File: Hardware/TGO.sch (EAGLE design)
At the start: 33 parts, among them J4 SMD_PAD, U1 AP3012, U2 SAS1-1U001-A_I2C_4WSPI

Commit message: Finish prototype v01
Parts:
- removed LOGO1: SFE_LOGO_NAME_FLAME.1_INCH, SparkFun-Aesthetics:SFE_LOGO_NAME_FLAME.1_INCH
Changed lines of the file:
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@@
 <part name="FD2" library="SparkFun-Aesthetics" deviceset="FIDUCIAL" device="1X2"/>
 <part name="FD4" library="SparkFun-Aesthetics" deviceset="FIDUCIAL" device="1X2"/>
-<part name="LOGO1" library="SparkFun-Aesthetics" deviceset="SFE_LOGO_NAME_FLAME" device=".1_INCH"/>
 <part name="LOGO2" library="SparkFun-Aesthetics" deviceset="OSHW-LOGO" device="S"/>
 <part name="J3" library="SparkFun-Connectors" deviceset="CONN_06" device="NO_SILK_NO_POP"/>
@@
 <instance part="FD2" gate="G$1" x="243.84" y="30.48"/>
 <instance part="FD4" gate="G$1" x="246.38" y="30.48"/>
-<instance part="LOGO1" gate="G$1" x="152.4" y="48.26"/>
 <instance part="LOGO2" gate="G$1" x="228.6" y="60.96"/>
 <instance part="J3" gate="G$1" x="111.76" y="22.86" rot="R180"/>

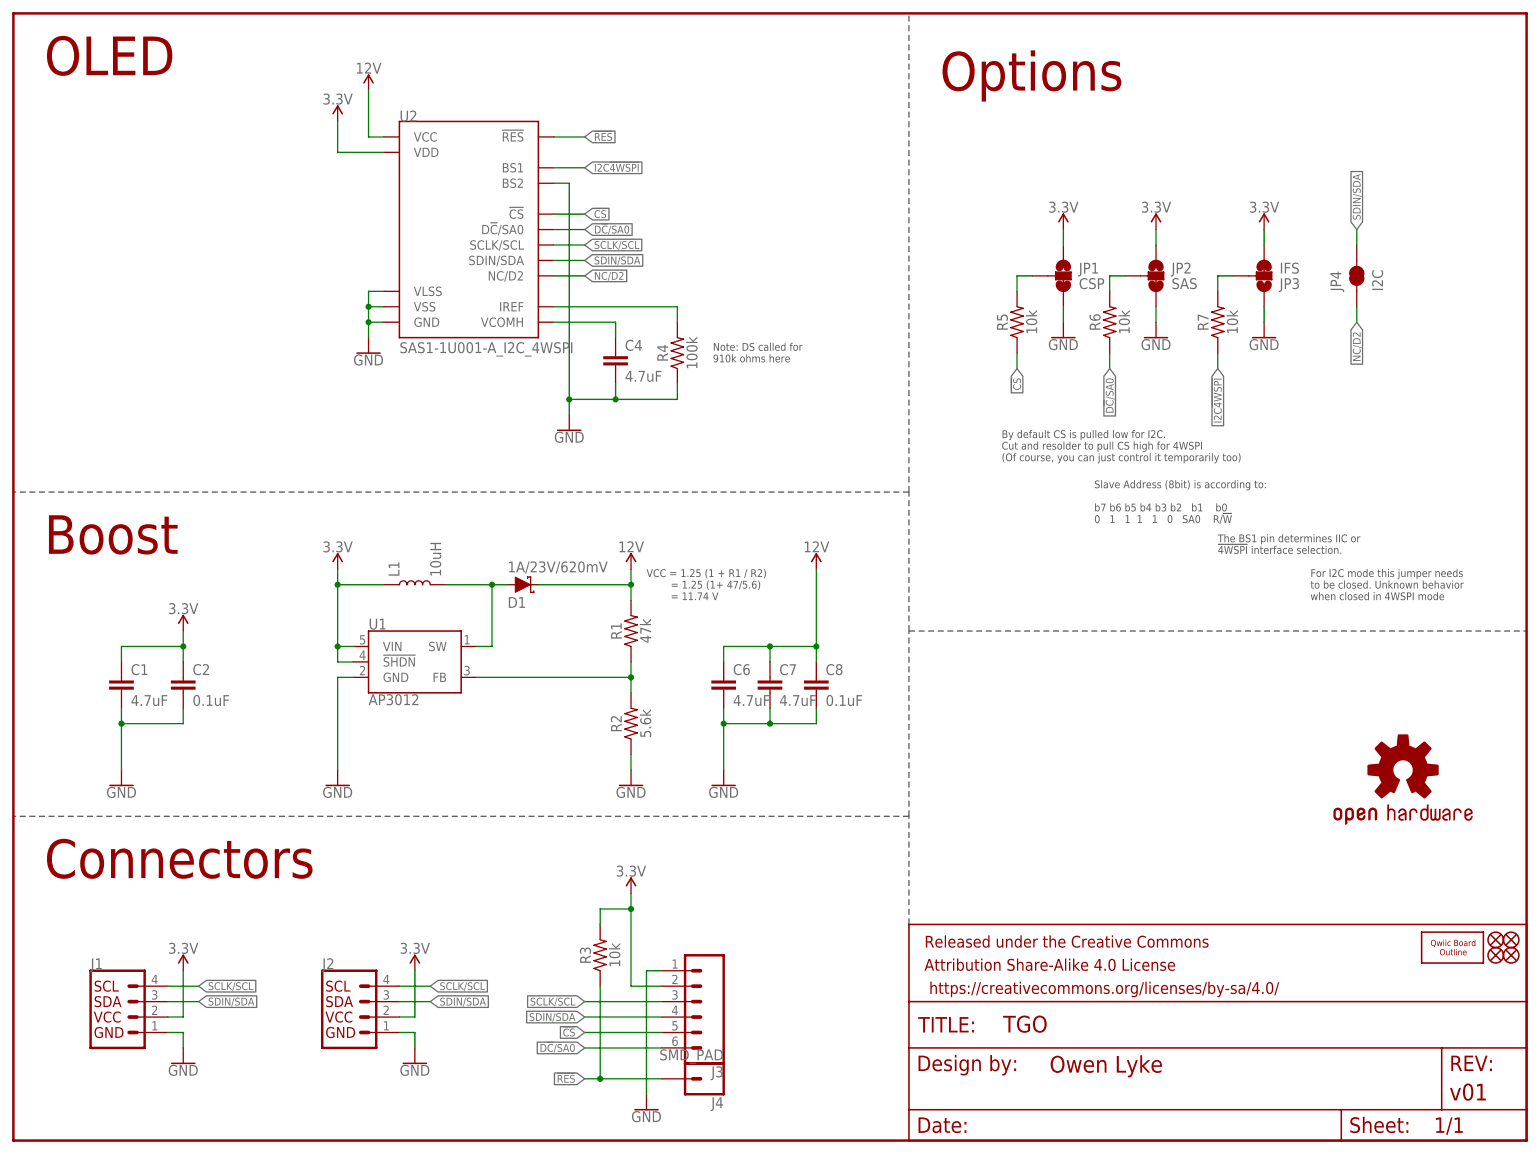
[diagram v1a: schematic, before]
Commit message: Proto review changes
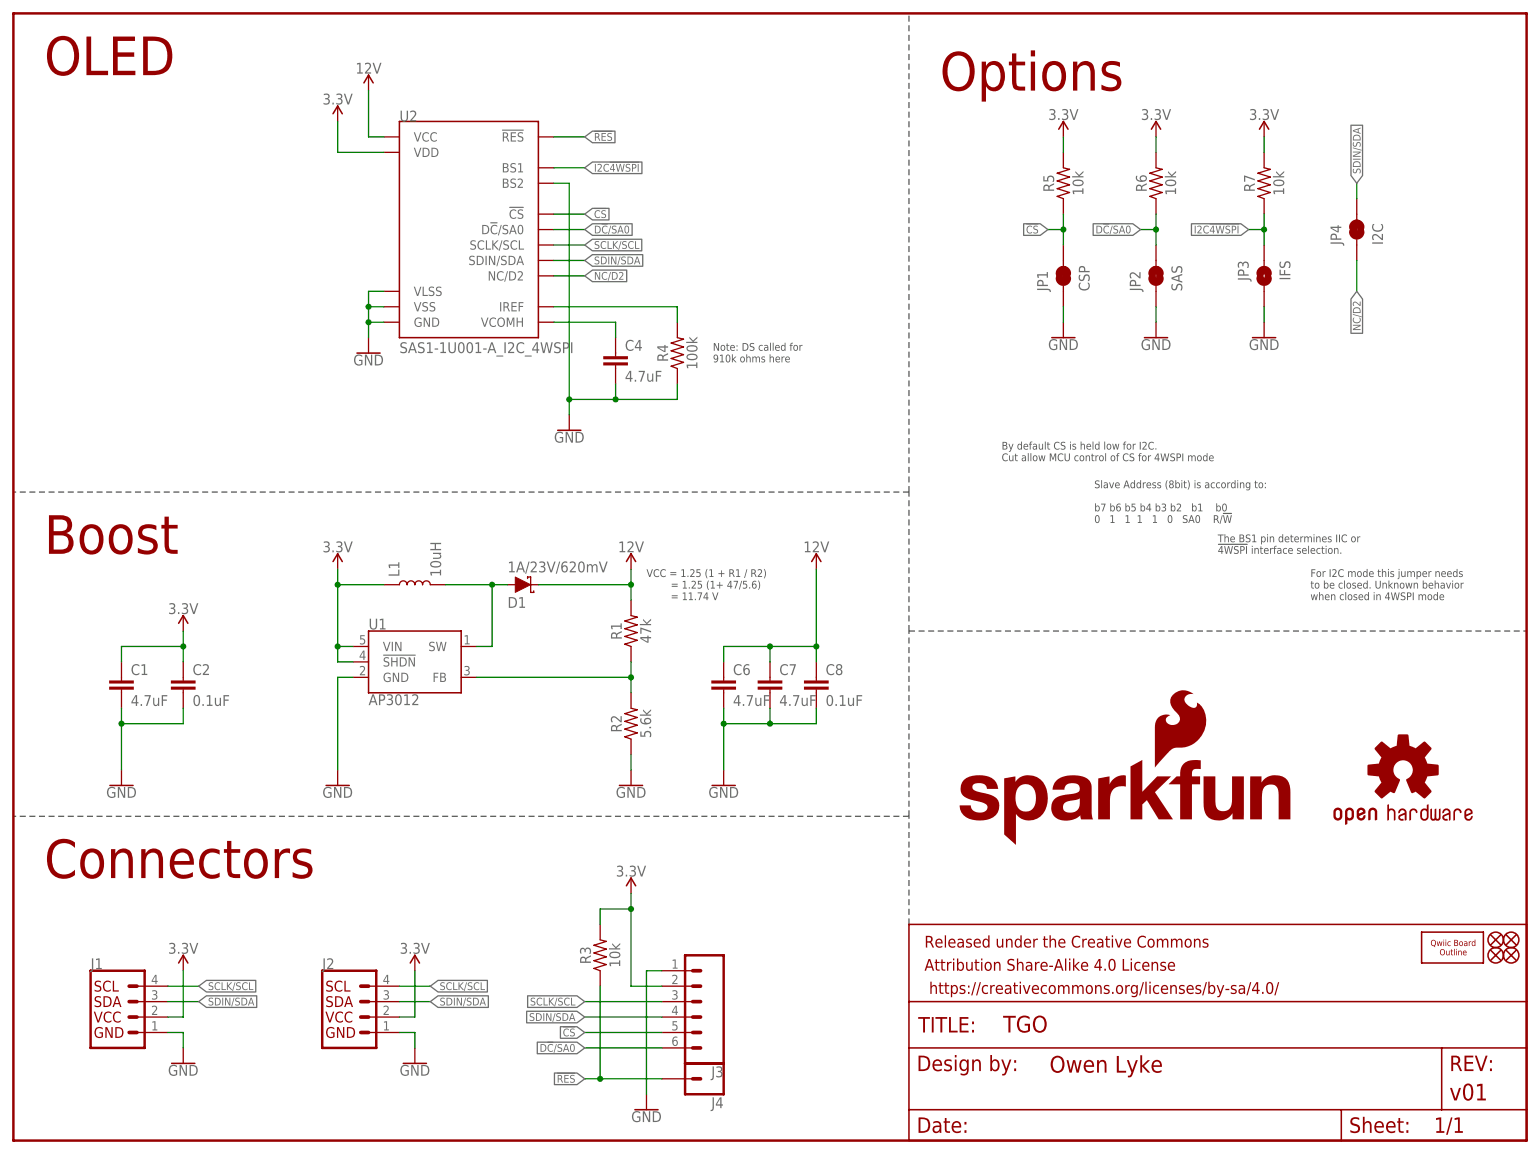
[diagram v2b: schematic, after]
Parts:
- added LOGO1: SFE_LOGO_NAME_FLAME.1_INCH, SparkFun-Aesthetics:SFE_LOGO_NAME_FLAME.1_INCH
- J4: value SMD_PAD -> (none); device TGO:SMD_PAD -> SparkFun-Connectors:CONN_01PTH_NO_SILK_YES_STOP
- JP1, JP2: device SparkFun-Jumpers:JUMPER-SMT_3_1-NC_TRACE_SILK -> SparkFun-Jumpers:JUMPER-SMT_2_NC_TRACE_SILK
- JP3: device SparkFun-Jumpers:JUMPER-SMT_3_1-NC_TRACE_SILK -> SparkFun-Jumpers:JUMPER-SMT_2_NO_SILK
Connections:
- removed net N$2: JP2.2, R6.2
- removed net N$6: JP1.2, R5.2
- removed net N$7: JP3.2, R7.2
- net !CS: now also JP1.2
- net 3.3V: now also R5.2, R6.2, R7.2; no longer JP1.1, JP2.1, JP3.3
- net D!C!/SA0: now also JP2.2
- net GND: now also JP1.1, JP2.1, JP3.2; no longer JP1.3, JP2.3, JP3.1
- net I2C!4WSPI: now also JP3.1
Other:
- note added: "By default CS is held low for I2C. Cut allow MCU control of CS for 4WSPI mode"
- note removed: "By default CS is pulled low for I2C. Cut and resolder to pull CS high for 4WSPI (Of course, you can just control it temporarily too)"
- moved on the sheet: JP4, R5, R6, R7

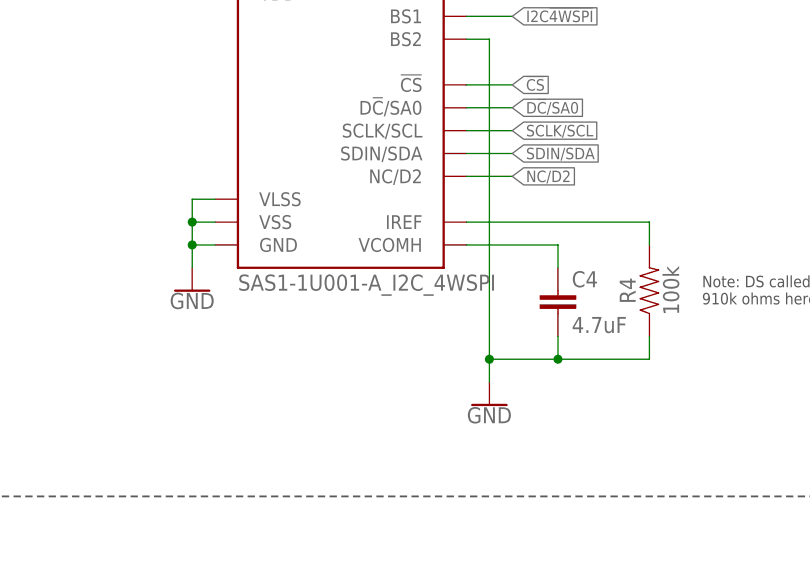
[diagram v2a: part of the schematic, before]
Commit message: Move display into SparkFun library
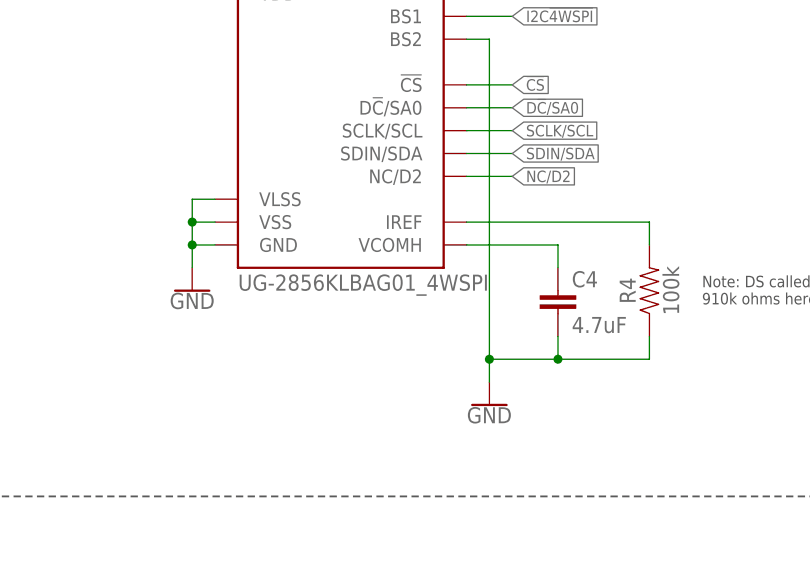
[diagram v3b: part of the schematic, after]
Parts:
- U2: value SAS1-1U001-A_I2C_4WSPI -> UG-2856KLBAG01_4WSPI; device TGO:SAS1-1U001-A_I2C_4WSPI -> SparkFun-Displays:UG-2856KLBAG01_4WSPI
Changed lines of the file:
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@@
 </classes>
 <parts>
-<part name="U2" library="TGO" deviceset="SAS1-1U001-A_I2C_4WSPI" device=""/>
+<part name="U2" library="SparkFun-Displays" deviceset="UG-2856KLBAG01_4WSPI" device=""/>
 <part name="GND5" library="SparkFun-PowerSymbols" deviceset="GND" device=""/>
 <part name="GND7" library="SparkFun-PowerSymbols" deviceset="GND" device=""/>

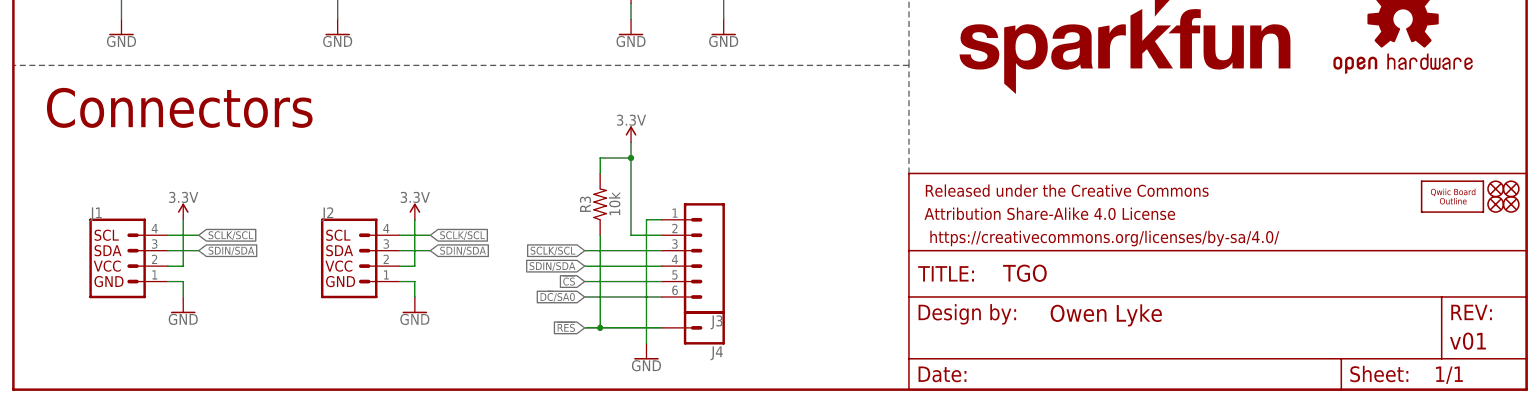
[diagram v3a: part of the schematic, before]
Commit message: Add pullup resistors on I2C lines, increment version number
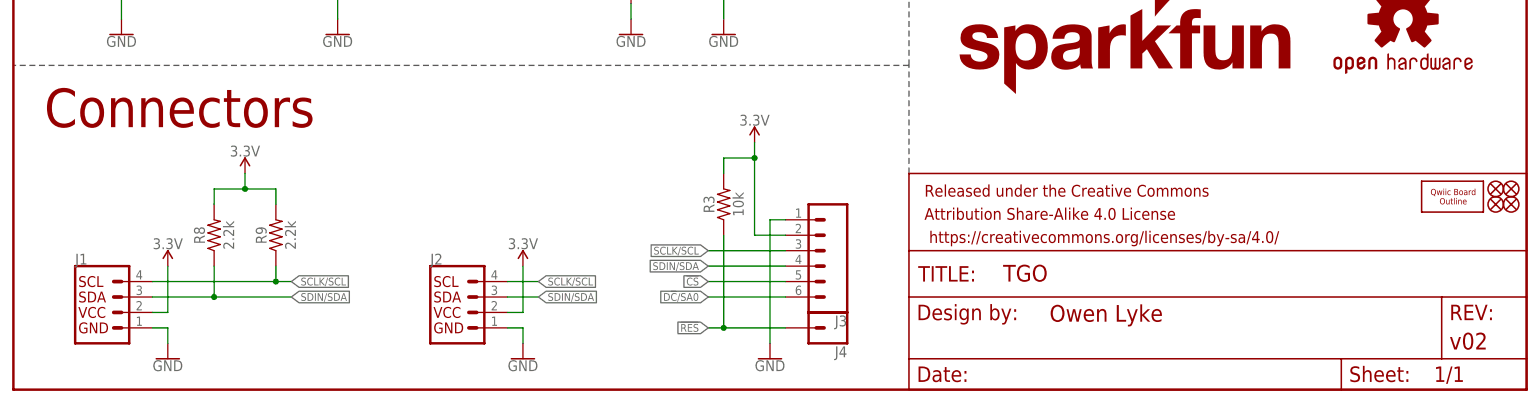
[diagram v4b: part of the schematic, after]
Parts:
- added R8, R9: 2.2k, SparkFun-Resistors:2.2KOHM-0603-1/10W-1%
- FRAME1: REV v01 -> v02
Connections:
- net 3.3V: now also R8.2, R9.2
- net SCLK/SCL: now also R9.1
- net SDIN/SDA: now also R8.1
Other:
- moved on the sheet: J1, J2, J3, J4, R3
